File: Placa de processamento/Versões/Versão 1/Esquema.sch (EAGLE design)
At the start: 15 parts, among them IC2 5V

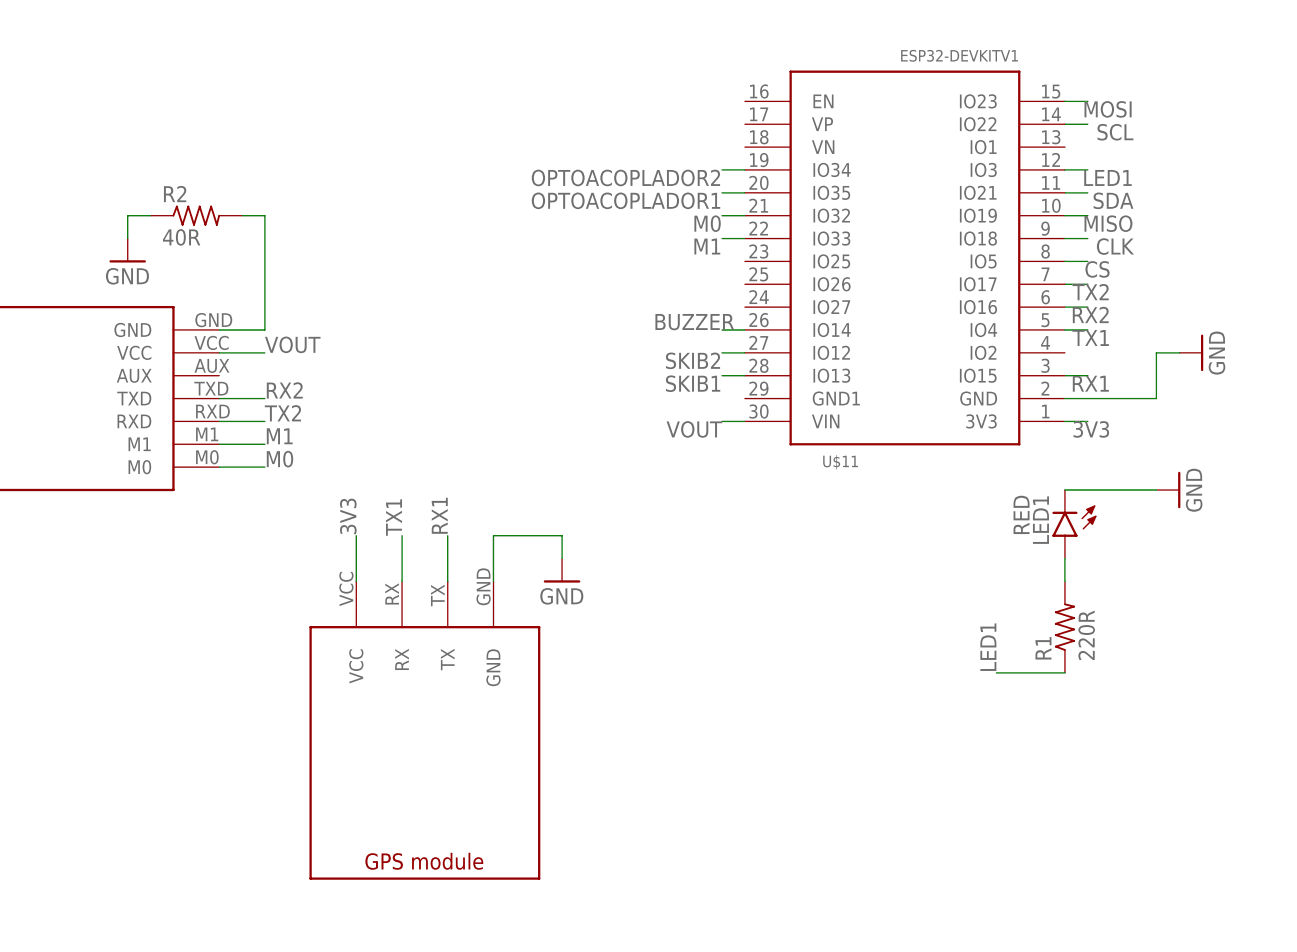
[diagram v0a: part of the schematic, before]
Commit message: mudanças na placa de processamento
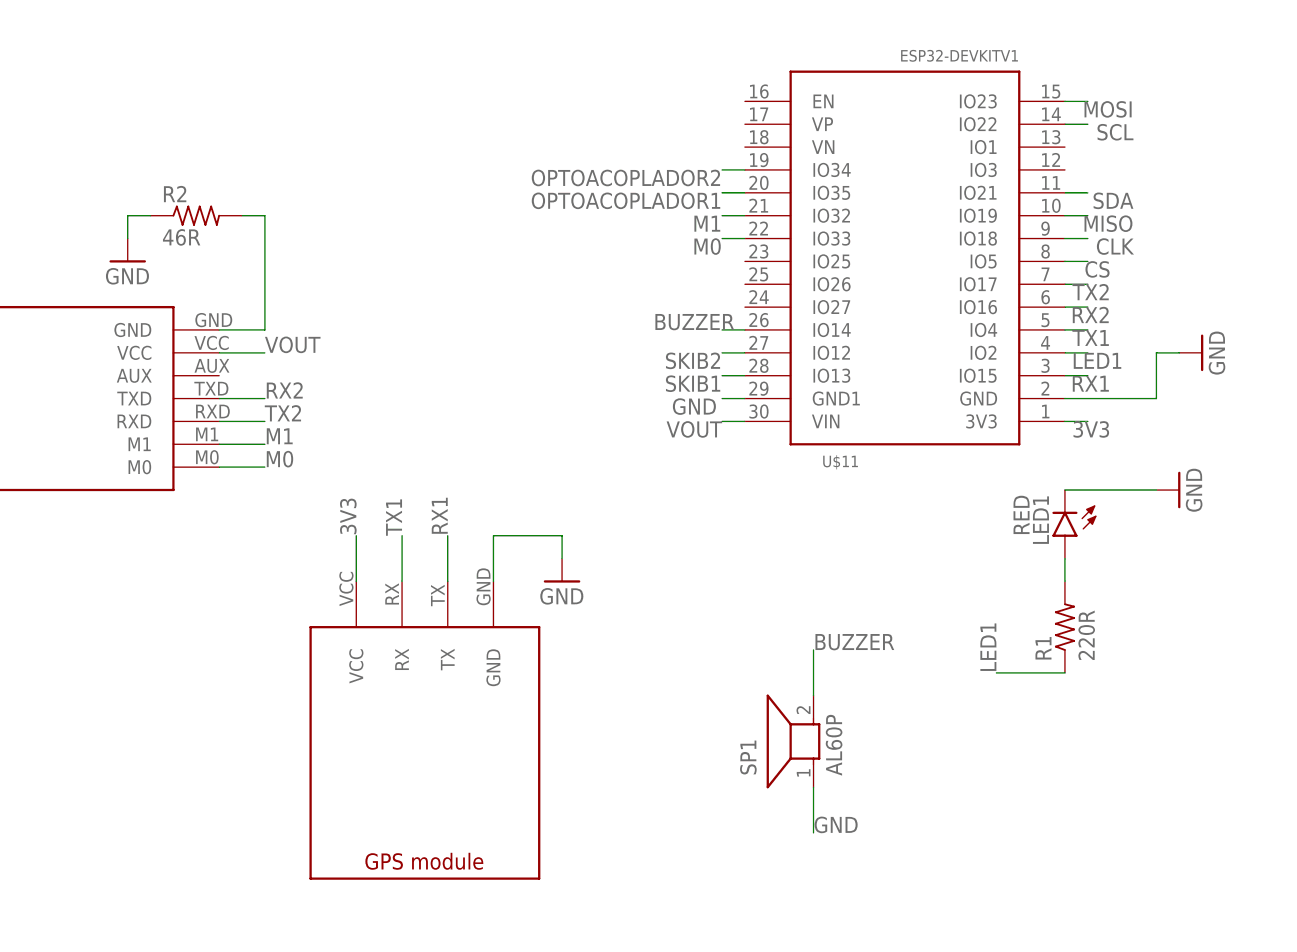
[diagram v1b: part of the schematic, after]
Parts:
- added SP1: AL60P, buzzer:AL60P
- R2: value 40R -> 46R
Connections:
- net BUZZER: now also SP1.2
- net GND: now also SP1.1, U$11.GND1
- net LED1: now also U$11.IO2; no longer U$11.IO3
- net M0: now also U$11.IO33; no longer U$11.IO32
- net M1: now also U$11.IO32; no longer U$11.IO33
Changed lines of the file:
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@@
 <drawing>
 <settings>
-<setting alwaysvectorfont="yes"/>
+<setting alwaysvectorfont="no"/>
 <setting verticaltext="up"/>
 </settings>
@@
 <part name="R1" library="rcl" library_urn="urn:adsk.eagle:library:334" deviceset="R-US_" device="0309/12" package3d_urn="urn:adsk.eagle:package:23571/1" value="220R"/>
 <part name="U$12" library="CRD" library_urn="urn:adsk.eagle:library:39051337" deviceset="CHAVE_SS-5GL" device="" package3d_urn="urn:adsk.eagle:package:45208058/6"/>
-<part name="R2" library="rcl" library_urn="urn:adsk.eagle:library:334" deviceset="R-US_" device="0309/12" package3d_urn="urn:adsk.eagle:package:23571/1" value="40R"/>
+<part name="R2" library="rcl" library_urn="urn:adsk.eagle:library:334" deviceset="R-US_" device="0309/12" package3d_urn="urn:adsk.eagle:package:23571/1" value="46R"/>
 <part name="GND1" library="supply1" library_urn="urn:adsk.eagle:library:371" deviceset="GND" device=""/>
 <part name="GND2" library="supply1" library_urn="urn:adsk.eagle:library:371" deviceset="GND" device=""/>
@@
 <part name="GND5" library="supply1" library_urn="urn:adsk.eagle:library:371" deviceset="GND" device=""/>
 <part name="GND6" library="supply1" library_urn="urn:adsk.eagle:library:371" deviceset="GND" device=""/>
+<part name="SP1" library="buzzer" library_urn="urn:adsk.eagle:library:113" deviceset="AL60P" device="" package3d_urn="urn:adsk.eagle:package:5261/1"/>
 </parts>
 <sheets>
@@
 <attribute name="VALUE" x="30.48" y="63.5" size="1.778" layer="96"/>
 </instance>
+<instance part="SP1" gate="G$1" x="66.04" y="-45.72" smashed="yes" rot="R90">
+<attribute name="NAME" x="59.69" y="-49.53" size="1.778" layer="95" rot="R90"/>
+<attribute name="VALUE" x="69.215" y="-49.53" size="1.778" layer="96" rot="R90"/>
+</instance>
 </instances>
 <busses>
@@
 <pinref part="GND6" gate="1" pin="GND"/>
 </segment>
+<segment>
+<pinref part="SP1" gate="G$1" pin="1"/>
+<wire x1="66.04" y1="-50.8" x2="66.04" y2="-55.88" width="0.1524" layer="91"/>
+<label x="66.04" y="-55.88" size="1.778" layer="95"/>
+</segment>
+<segment>
+<pinref part="U$11" gate="G$1" pin="GND1"/>
+<wire x1="58.42" y1="-7.62" x2="55.88" y2="-7.62" width="0.1524" layer="91"/>
+<label x="50.292" y="-9.398" size="1.778" layer="95"/>
+</segment>
 </net>
 <net name="N$4" class="0">
@@
 </segment>
 <segment>
+<pinref part="U$11" gate="G$1" pin="IO32"/>
+<wire x1="58.42" y1="12.7" x2="55.88" y2="12.7" width="0.1524" layer="91"/>
+<label x="55.88" y="12.7" size="1.778" layer="95" rot="R180"/>
+</segment>
+</net>
+<net name="M0" class="0">
+<segment>
+<pinref part="U$2" gate="LORA_E22400T30D" pin="M0"/>
+<wire x1="0" y1="-15.24" x2="5.08" y2="-15.24" width="0.1524" layer="91"/>
+<label x="5.08" y="-15.24" size="1.778" layer="95"/>
+</segment>
+<segment>
 <pinref part="U$11" gate="G$1" pin="IO33"/>
 <wire x1="58.42" y1="10.16" x2="55.88" y2="10.16" width="0.1524" layer="91"/>
@@
 </segment>
 </net>
-<net name="M0" class="0">
-<segment>
-<pinref part="U$2" gate="LORA_E22400T30D" pin="M0"/>
-<wire x1="0" y1="-15.24" x2="5.08" y2="-15.24" width="0.1524" layer="91"/>
-<label x="5.08" y="-15.24" size="1.778" layer="95"/>
-</segment>
-<segment>
-<pinref part="U$11" gate="G$1" pin="IO32"/>
-<wire x1="58.42" y1="12.7" x2="55.88" y2="12.7" width="0.1524" layer="91"/>
-<label x="55.88" y="12.7" size="1.778" layer="95" rot="R180"/>
-</segment>
-</net>
 <net name="3V3" class="0">
 <segment>
@@
 </segment>
 <segment>
-<pinref part="U$11" gate="G$1" pin="IO3"/>
-<wire x1="93.98" y1="17.78" x2="96.52" y2="17.78" width="0.1524" layer="91"/>
-<label x="101.6" y="17.78" size="1.778" layer="95" rot="R180"/>
+<pinref part="U$11" gate="G$1" pin="IO2"/>
+<wire x1="93.98" y1="-2.54" x2="96.52" y2="-2.54" width="0.1524" layer="91"/>
+<label x="94.742" y="-4.318" size="1.778" layer="95"/>
 </segment>
 </net>
@@
 <label x="48.26" y="0" size="1.778" layer="95"/>
 </segment>
-</net>
+<segment>
+<pinref part="SP1" gate="G$1" pin="2"/>
+<wire x1="66.04" y1="-40.64" x2="66.04" y2="-35.56" width="0.1524" layer="91"/>
+<label x="66.04" y="-35.56" size="1.778" layer="95"/>
+</segment>
+</net>

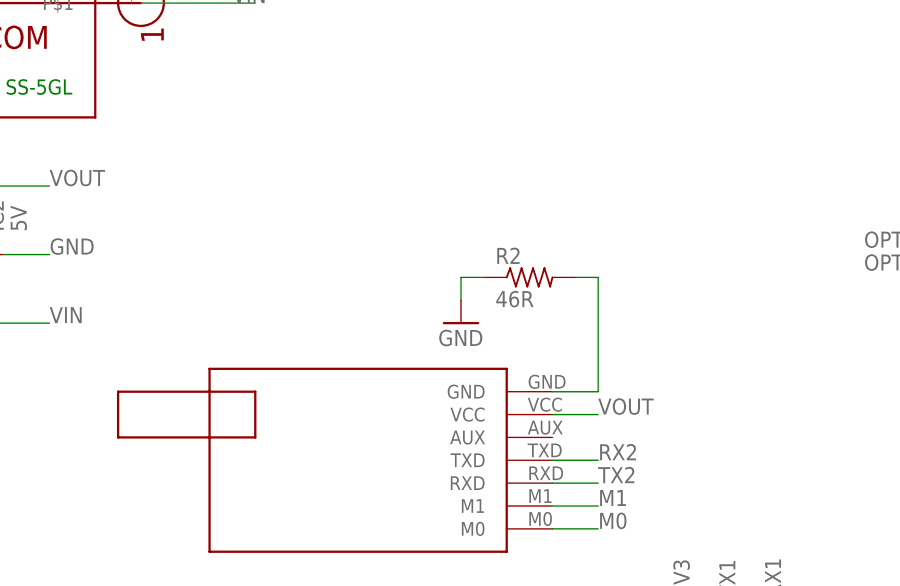
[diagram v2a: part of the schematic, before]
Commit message: atualização de regulador
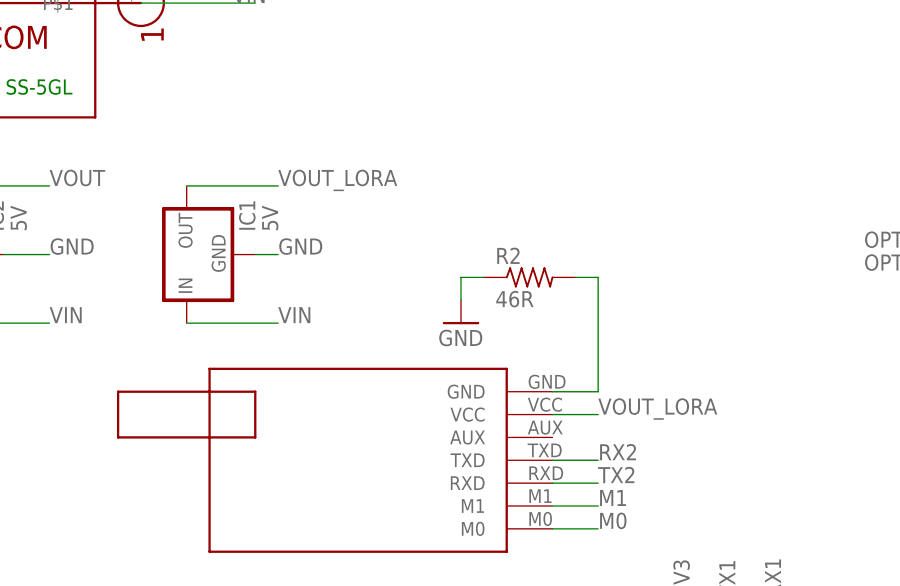
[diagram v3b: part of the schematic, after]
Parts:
- added IC1: 5V, v-reg:78XXL
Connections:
- new net VOUT_LORA: IC1.OUT, U$2.VCC
- net GND: now also IC1.GND
- net VIN: now also IC1.IN
- net VOUT: no longer U$2.VCC
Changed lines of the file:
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@@
 <part name="GND6" library="supply1" library_urn="urn:adsk.eagle:library:371" deviceset="GND" device=""/>
 <part name="SP1" library="buzzer" library_urn="urn:adsk.eagle:library:113" deviceset="AL60P" device="" package3d_urn="urn:adsk.eagle:package:5261/1"/>
+<part name="IC1" library="v-reg" library_urn="urn:adsk.eagle:library:409" deviceset="78XXL" device="" package3d_urn="urn:adsk.eagle:package:30361/1" value="5V"/>
 </parts>
 <sheets>
@@
 <attribute name="VALUE" x="69.215" y="-49.53" size="1.778" layer="96" rot="R90"/>
 </instance>
+<instance part="IC1" gate="A" x="-40.64" y="15.24" smashed="yes" rot="R90">
+<attribute name="NAME" x="-33.02" y="17.78" size="1.778" layer="95" rot="R90"/>
+<attribute name="VALUE" x="-30.48" y="17.78" size="1.778" layer="96" rot="R90"/>
+</instance>
 </instances>
 <busses>
@@
 <label x="-55.88" y="7.62" size="1.778" layer="95"/>
 </segment>
+<segment>
+<pinref part="IC1" gate="A" pin="IN"/>
+<wire x1="-40.64" y1="7.62" x2="-30.48" y2="7.62" width="0.1524" layer="91"/>
+<label x="-30.48" y="7.62" size="1.778" layer="95"/>
+</segment>
 </net>
 <net name="V_BATTERY" class="0">
@@
 <label x="50.292" y="-9.398" size="1.778" layer="95"/>
 </segment>
+<segment>
+<pinref part="IC1" gate="A" pin="GND"/>
+<wire x1="-33.02" y1="15.24" x2="-30.48" y2="15.24" width="0.1524" layer="91"/>
+<label x="-30.48" y="15.24" size="1.778" layer="95"/>
+</segment>
 </net>
 <net name="N$4" class="0">
@@
 <wire x1="-68.58" y1="22.86" x2="-55.88" y2="22.86" width="0.1524" layer="91"/>
 <label x="-55.88" y="22.86" size="1.778" layer="95"/>
-</segment>
-<segment>
-<pinref part="U$2" gate="LORA_E22400T30D" pin="VCC"/>
-<wire x1="5.08" y1="-2.54" x2="0" y2="-2.54" width="0.1524" layer="91"/>
-<label x="5.08" y="-2.54" size="1.778" layer="95"/>
 </segment>
 </net>
@@
 </segment>
 </net>
+<net name="VOUT_LORA" class="0">
+<segment>
+<pinref part="IC1" gate="A" pin="OUT"/>
+<wire x1="-40.64" y1="22.86" x2="-30.48" y2="22.86" width="0.1524" layer="91"/>
+<label x="-30.48" y="22.86" size="1.778" layer="95"/>
+</segment>
+<segment>
+<pinref part="U$2" gate="LORA_E22400T30D" pin="VCC"/>
+<wire x1="5.08" y1="-2.54" x2="0" y2="-2.54" width="0.1524" layer="91"/>
+<label x="5.08" y="-2.54" size="1.778" layer="95"/>
+</segment>
+</net>

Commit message: uptate boards
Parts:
- removed IC1: 5V, v-reg:78XXL
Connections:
- removed net VOUT_LORA: IC1.OUT, U$2.VCC
- net GND: no longer IC1.GND
- net VIN: no longer IC1.IN
- net VOUT: now also U$2.VCC
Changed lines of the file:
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@@
 <part name="GND6" library="supply1" library_urn="urn:adsk.eagle:library:371" deviceset="GND" device=""/>
 <part name="SP1" library="buzzer" library_urn="urn:adsk.eagle:library:113" deviceset="AL60P" device="" package3d_urn="urn:adsk.eagle:package:5261/1"/>
-<part name="IC1" library="v-reg" library_urn="urn:adsk.eagle:library:409" deviceset="78XXL" device="" package3d_urn="urn:adsk.eagle:package:30361/1" value="5V"/>
 </parts>
 <sheets>
@@
 <attribute name="VALUE" x="69.215" y="-49.53" size="1.778" layer="96" rot="R90"/>
 </instance>
-<instance part="IC1" gate="A" x="-40.64" y="15.24" smashed="yes" rot="R90">
-<attribute name="NAME" x="-33.02" y="17.78" size="1.778" layer="95" rot="R90"/>
-<attribute name="VALUE" x="-30.48" y="17.78" size="1.778" layer="96" rot="R90"/>
-</instance>
 </instances>
 <busses>
@@
 <label x="-55.88" y="7.62" size="1.778" layer="95"/>
 </segment>
-<segment>
-<pinref part="IC1" gate="A" pin="IN"/>
-<wire x1="-40.64" y1="7.62" x2="-30.48" y2="7.62" width="0.1524" layer="91"/>
-<label x="-30.48" y="7.62" size="1.778" layer="95"/>
-</segment>
 </net>
 <net name="V_BATTERY" class="0">
@@
 <label x="50.292" y="-9.398" size="1.778" layer="95"/>
 </segment>
-<segment>
-<pinref part="IC1" gate="A" pin="GND"/>
-<wire x1="-33.02" y1="15.24" x2="-30.48" y2="15.24" width="0.1524" layer="91"/>
-<label x="-30.48" y="15.24" size="1.778" layer="95"/>
-</segment>
 </net>
 <net name="N$4" class="0">
@@
 <wire x1="-68.58" y1="22.86" x2="-55.88" y2="22.86" width="0.1524" layer="91"/>
 <label x="-55.88" y="22.86" size="1.778" layer="95"/>
+</segment>
+<segment>
+<pinref part="U$2" gate="LORA_E22400T30D" pin="VCC"/>
+<wire x1="5.08" y1="-2.54" x2="0" y2="-2.54" width="0.1524" layer="91"/>
+<label x="5.08" y="-2.54" size="1.778" layer="95"/>
 </segment>
 </net>
@@
 </segment>
 </net>
-<net name="VOUT_LORA" class="0">
-<segment>
-<pinref part="IC1" gate="A" pin="OUT"/>
-<wire x1="-40.64" y1="22.86" x2="-30.48" y2="22.86" width="0.1524" layer="91"/>
-<label x="-30.48" y="22.86" size="1.778" layer="95"/>
-</segment>
-<segment>
-<pinref part="U$2" gate="LORA_E22400T30D" pin="VCC"/>
-<wire x1="5.08" y1="-2.54" x2="0" y2="-2.54" width="0.1524" layer="91"/>
-<label x="5.08" y="-2.54" size="1.778" layer="95"/>
-</segment>
-</net>
